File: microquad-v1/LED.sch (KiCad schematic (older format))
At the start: 2 parts

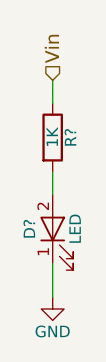
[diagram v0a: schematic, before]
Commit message: Changed LED resistor values
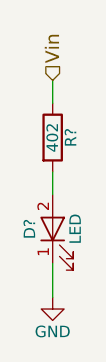
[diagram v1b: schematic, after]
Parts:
- R?: value 1K -> 402
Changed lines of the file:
@@
 P 4850 2700
 F 0 "R?" V 4930 2700 50  0000 C CNN
-F 1 "1K" V 4850 2700 50  0000 C CNN
+F 1 "402" V 4850 2700 50  0000 C CNN
 F 2 "" V 4780 2700 50  0001 C CNN
 F 3 "" H 4850 2700 50  0001 C CNN
